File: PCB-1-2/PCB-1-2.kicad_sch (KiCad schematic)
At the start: 79 parts, among them J1 Bus_PCI_Express_x8, J2 ST STDC14 (Debug Connector), J3 USB4105-GF-A, P1 USB_C_Plug_USB2.0, U1 LTC1298IS8_PBF, U10 INA827AIDGKR, U11 LTC1250CS8-PBF, U12 REF3425MDBVTEP, U13 HI-3585APQI, U2 LTC1451IS8-PBF, U3 HI-3110PSIF, U4 FT231XS-R, U5 STM32F103RBT6, U6 STWD100YNXWY3F, U7 ADP7104ACPZ-R7 (v3.3), U8 OPA2187IDGKR, U9 ADP7104ACPZ-R7 (5v), Y1 8MHz Crystal

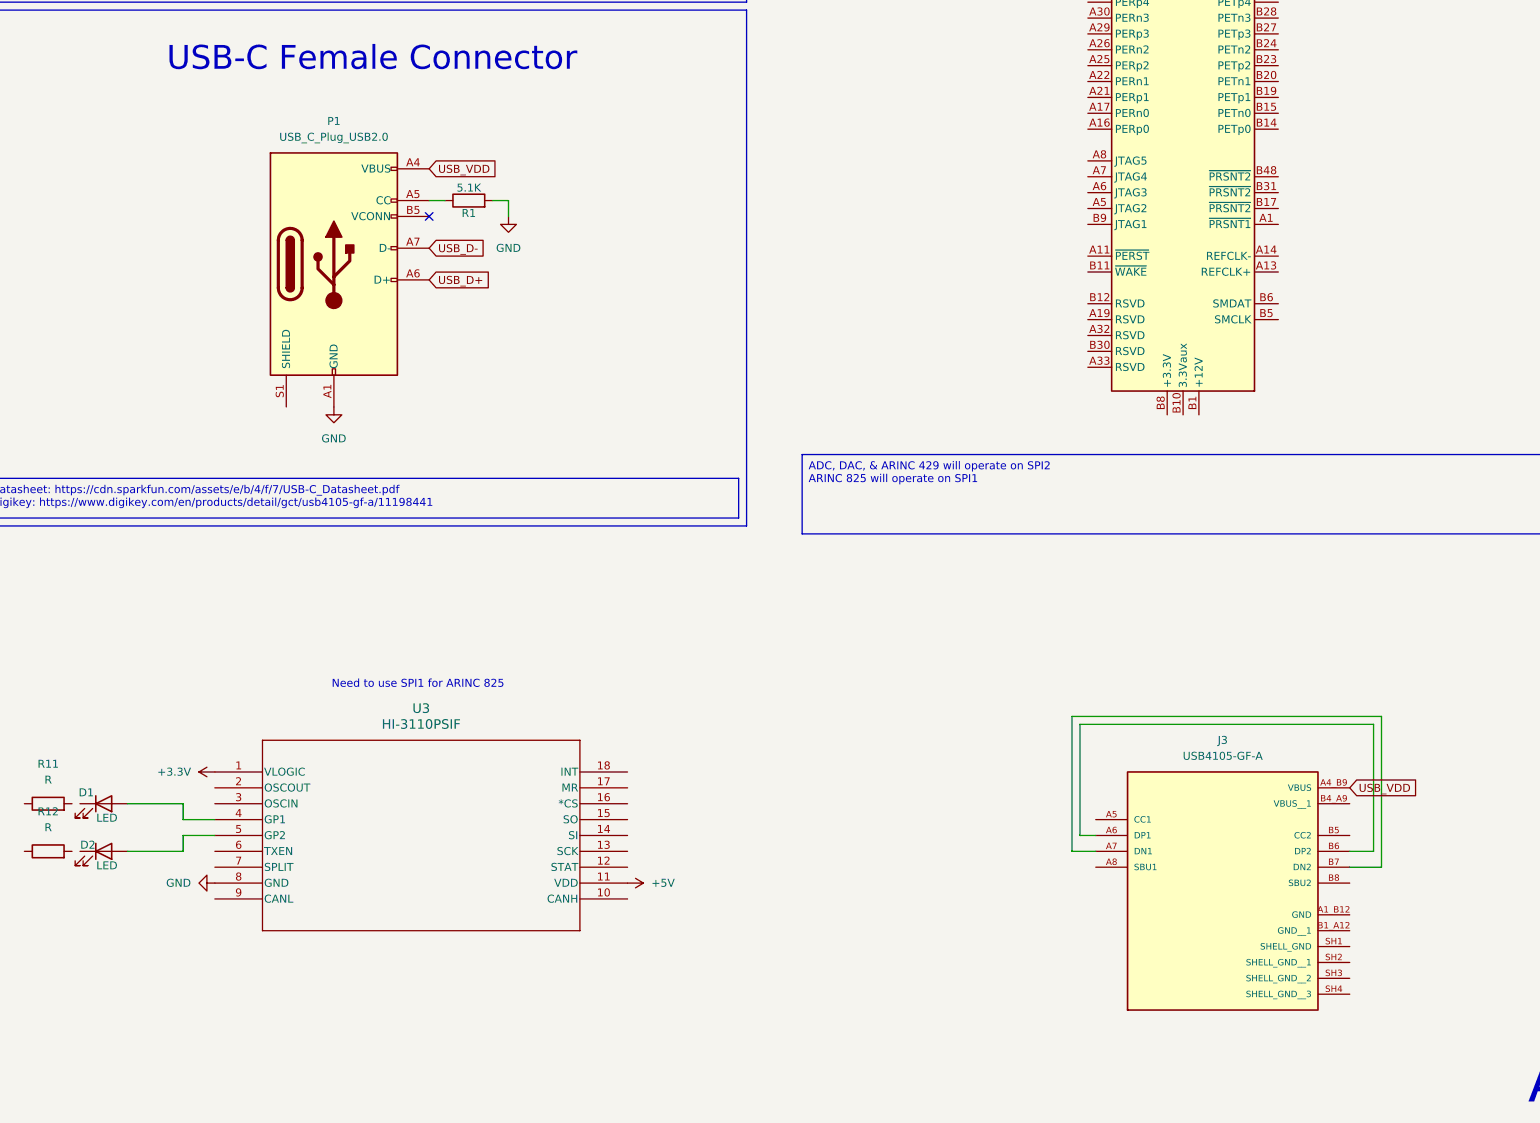
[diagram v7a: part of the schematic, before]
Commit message: Fixed/Updated the USB-C schematic
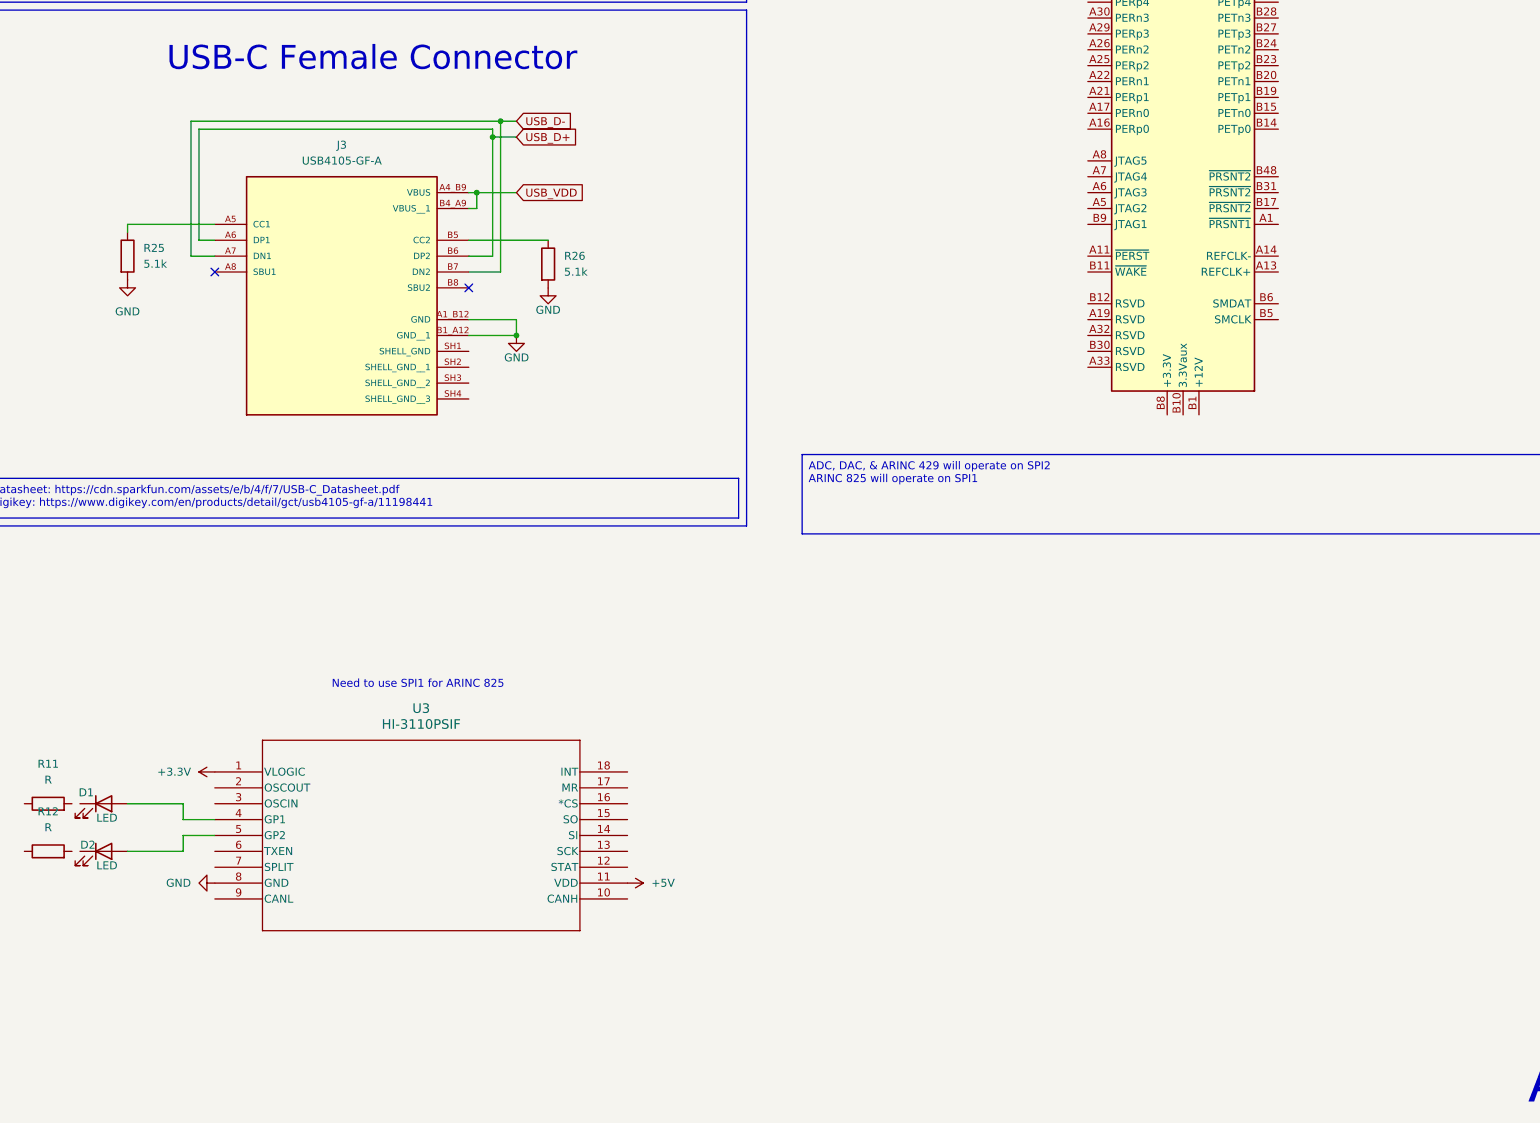
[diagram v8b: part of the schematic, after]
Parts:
- removed P1: USB_C_Plug_USB2.0, symbol Connector:USB_C_Plug_USB2.0
- removed R1: 5.1K, Resistor_SMD:R_0805_2012Metric, symbol Device:R
- added R25, R26: 5.1k, symbol Device:R
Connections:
- net GND: now also J3.A1_B12 (GND), J3.B1_A12 (GND__1), R25.2, R26.2
- net USB_D+: now also J3.A6 (DP1), J3.B6 (DP2)
- net USB_D-: now also J3.A7 (DN1), J3.B7 (DN2)
- net USB_VDD: now also J3.B4_A9 (VBUS__1)
- net at J3.A5 (CC1): now also R25.1
- net at J3.B5 (CC2): now also R26.1
- no-connect marks 22 -> 23
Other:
- moved on the sheet: J3
